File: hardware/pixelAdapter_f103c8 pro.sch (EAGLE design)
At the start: 52 parts, among them Q3 2.5A/30V/105mΩ, U1 SN74HCT245PWR, U2 AP2120N-3.3TRG1

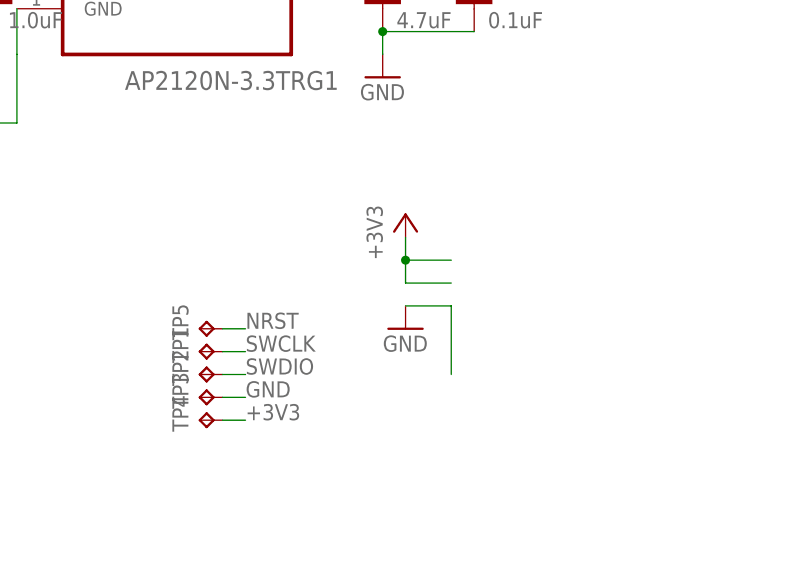
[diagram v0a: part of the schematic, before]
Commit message: remove some unused symbols
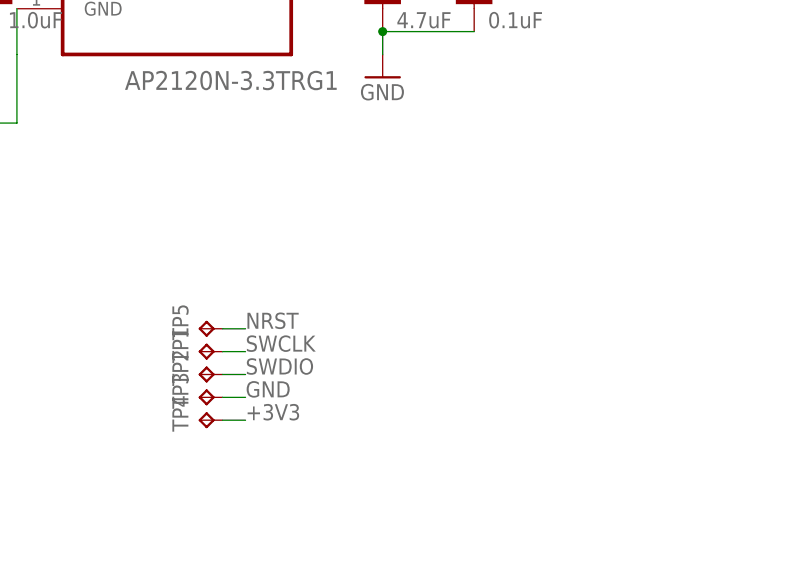
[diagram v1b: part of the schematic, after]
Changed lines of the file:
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@@
 <part name="GND2" library="supply1" deviceset="GND" device=""/>
 <part name="SUPPLY2" library="SparkFun-PowerSymbols" library_urn="urn:adsk.eagle:library:530" deviceset="5V" device=""/>
-<part name="+3V5" library="supply1" deviceset="+3V3" device=""/>
-<part name="GND6" library="supply1" deviceset="GND" device=""/>
 <part name="C3" library="SparkFun-Capacitors" library_urn="urn:adsk.eagle:library:510" deviceset="0.1UF" device="-0603-25V-(+80/-20%)" package3d_urn="urn:adsk.eagle:package:37414/1" value="0.1uF"/>
 <part name="GND1" library="supply1" deviceset="GND" device=""/>
@@
 <attribute name="VALUE" x="91.44" y="51.054" size="1.778" layer="96" rot="MR0" align="bottom-center"/>
 </instance>
-<instance part="+3V5" gate="G$1" x="33.02" y="58.42" smashed="yes">
-<attribute name="VALUE" x="30.48" y="53.34" size="1.778" layer="96" rot="R90"/>
-</instance>
-<instance part="GND6" gate="1" x="33.02" y="45.72" smashed="yes">
-<attribute name="VALUE" x="30.48" y="43.18" size="1.778" layer="96"/>
-</instance>
 <instance part="C3" gate="G$1" x="40.64" y="81.28" smashed="yes">
 <attribute name="NAME" x="42.164" y="84.201" size="1.778" layer="95" font="vector"/>
@@
 <pinref part="GND10" gate="1" pin="GND"/>
 <wire x1="30.48" y1="139.7" x2="30.48" y2="144.78" width="0.1524" layer="91"/>
-</segment>
-<segment>
-<pinref part="GND6" gate="1" pin="GND"/>
-<wire x1="33.02" y1="48.26" x2="38.1" y2="48.26" width="0.1524" layer="91"/>
-<wire x1="38.1" y1="40.64" x2="38.1" y2="48.26" width="0.1524" layer="91"/>
 </segment>
 <segment>
@@
 </segment>
 <segment>
-<pinref part="+3V5" gate="G$1" pin="+3V3"/>
-<wire x1="33.02" y1="50.8" x2="33.02" y2="53.34" width="0.1524" layer="91"/>
-<wire x1="33.02" y1="53.34" x2="33.02" y2="55.88" width="0.1524" layer="91"/>
-<wire x1="38.1" y1="50.8" x2="33.02" y2="50.8" width="0.1524" layer="91"/>
-<wire x1="38.1" y1="53.34" x2="33.02" y2="53.34" width="0.1524" layer="91"/>
-<junction x="33.02" y="53.34"/>
-</segment>
-<segment>

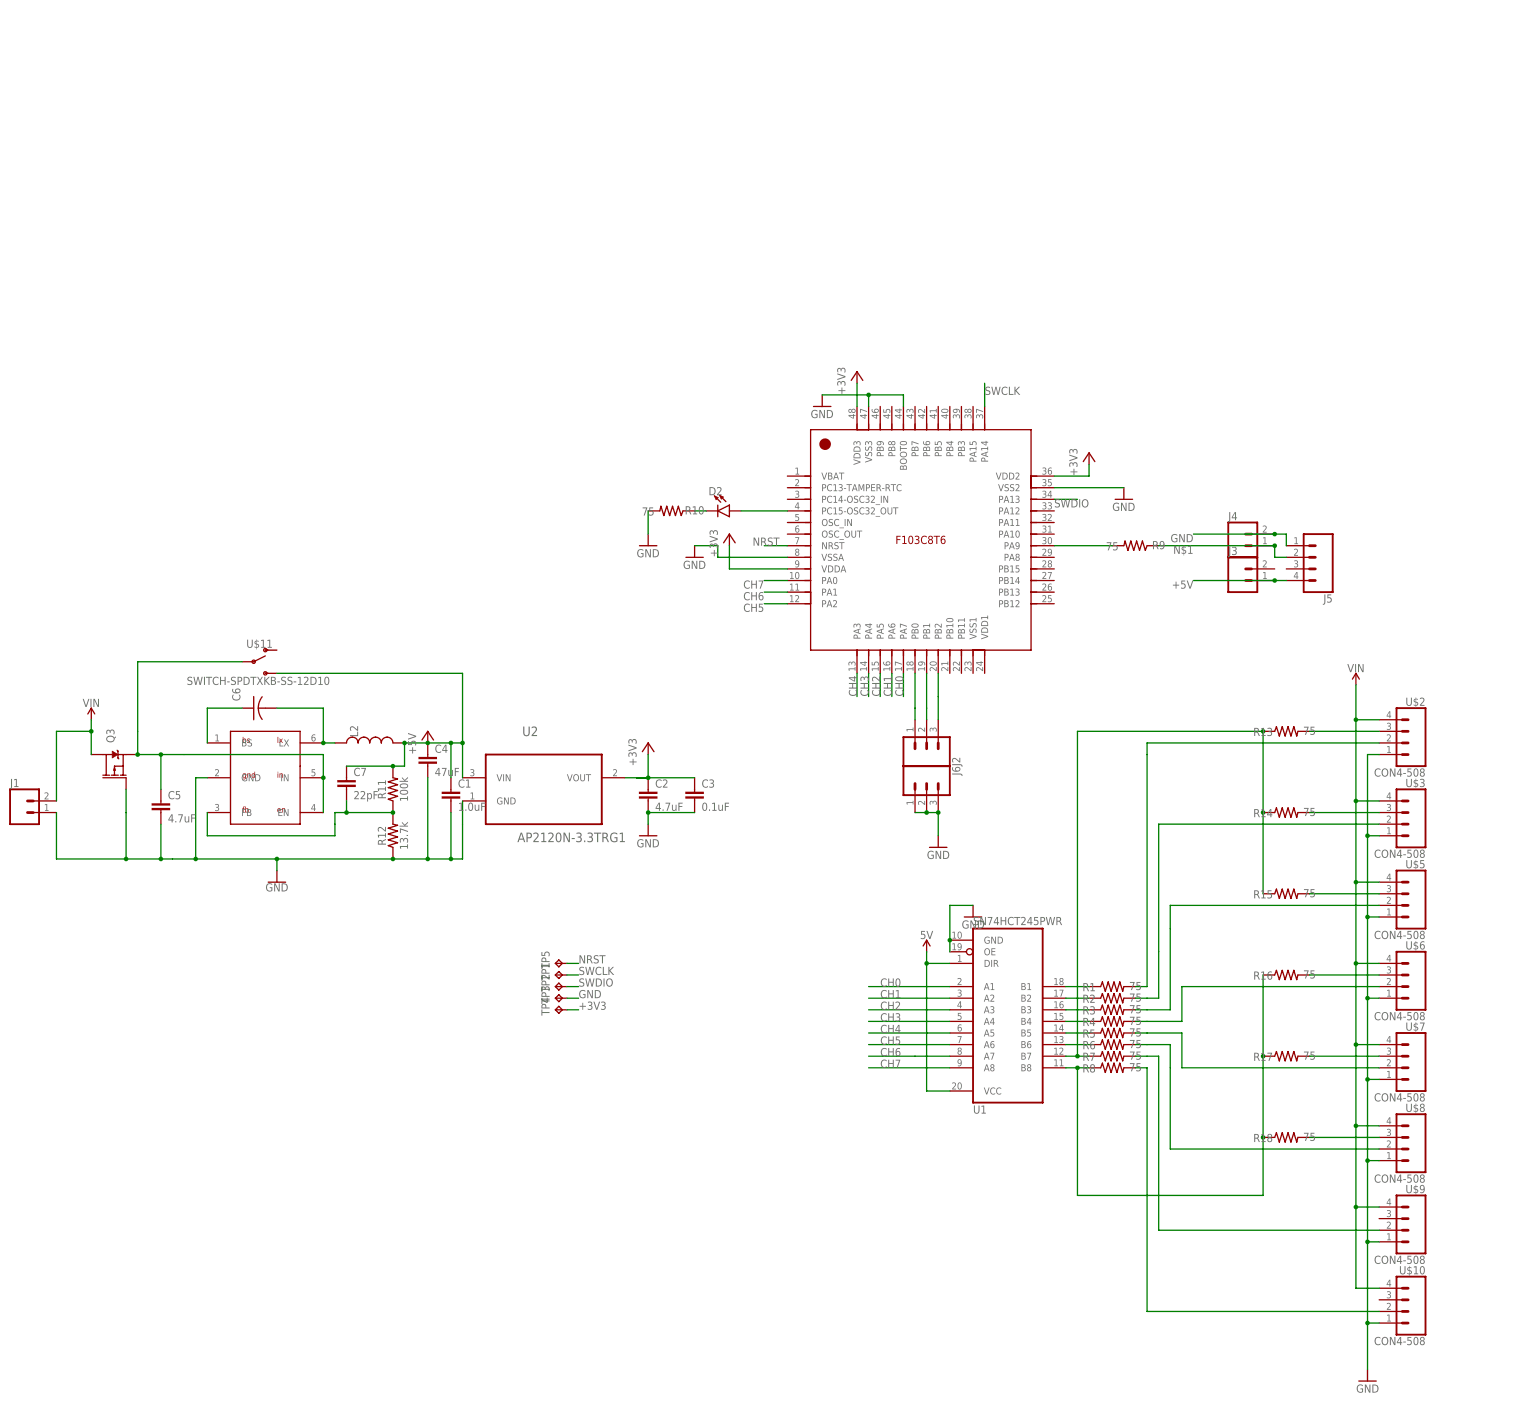
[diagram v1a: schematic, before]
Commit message: clean up schematics a little, get pdfs
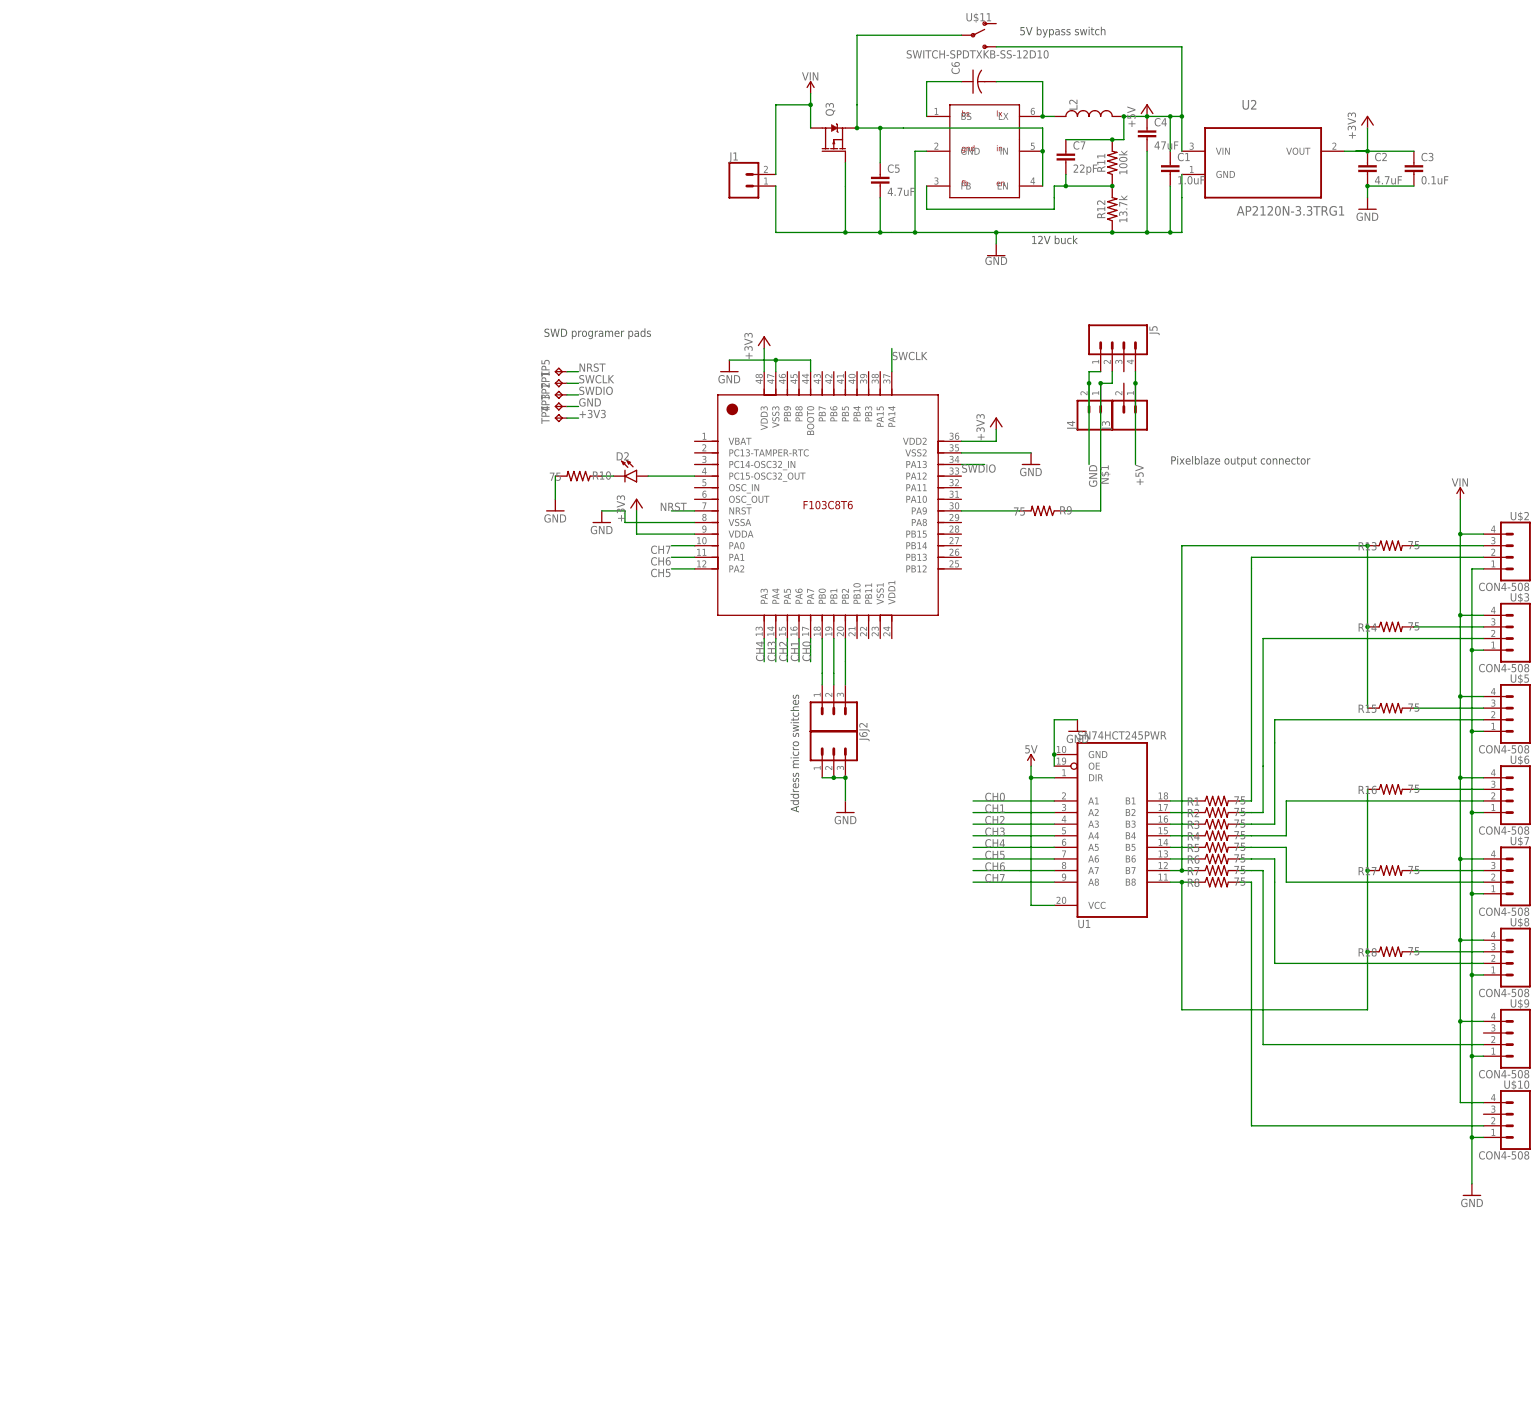
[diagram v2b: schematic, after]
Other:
- note added: "12V buck"
- note added: "5V bypass switch"
- note added: "Address micro switches"
- note added: "Pixelblaze output connector"
- note added: "SWD programer pads"
- moved on the sheet: C1, C2, C3, C4, C5, C6, C7, D2, J1, J2, J3, J4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
